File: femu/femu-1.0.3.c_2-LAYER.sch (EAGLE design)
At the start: 74 parts, among them IC1 ESP32-QFN_5X5

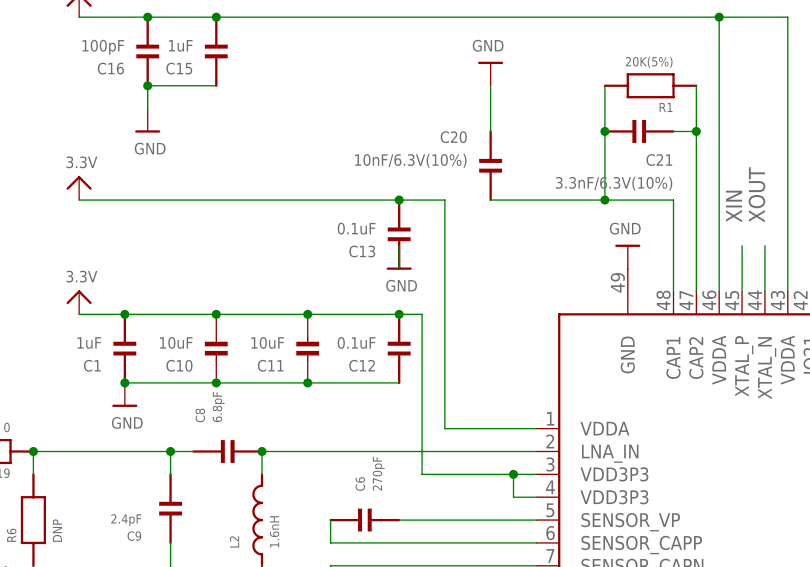
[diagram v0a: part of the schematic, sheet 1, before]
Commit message: Adding work on femu 1.0.2, and 1.0.3
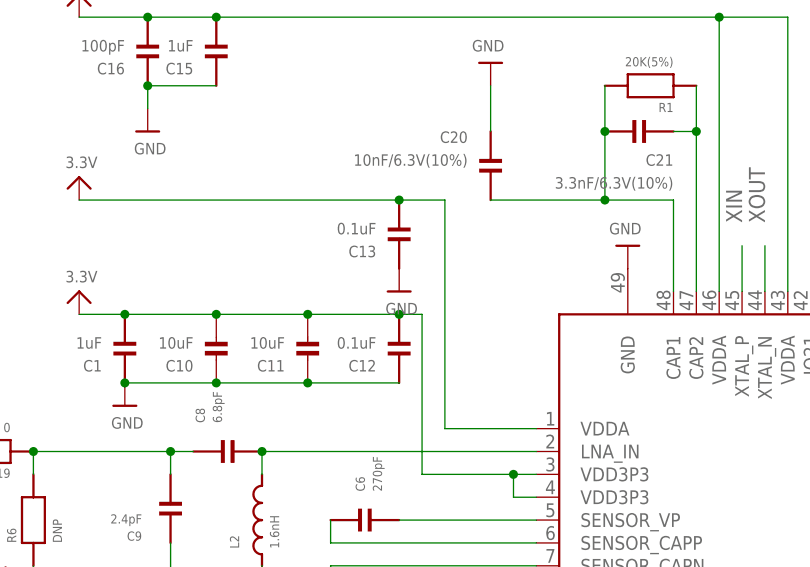
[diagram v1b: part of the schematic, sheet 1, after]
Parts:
- C13: MPN GRM022R60G104ME15L -> GRM033R61C104KE84D
- C23: MPN GRM035R60G475ME15D -> GRM035R60J475ME15D
- renumbered U$11 to IC2, U$57 to LDO2
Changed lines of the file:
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@@
 <part name="U$15" library="microbuilder" deviceset="GND" device=""/>
 <part name="C13" library="parts_0201" deviceset="CAPACITOR_0201" device="" value="0.1uF">
-<attribute name="MPN" value="GRM022R60G104ME15L"/>
+<attribute name="MPN" value="GRM033R61C104KE84D"/>
 </part>
 <part name="U$16" library="microbuilder" deviceset="GND" device=""/>
@@
 </part>
 <part name="C23" library="parts_0201" deviceset="CAPACITOR_0201" device="" value="4.7uF">
-<attribute name="MPN" value="GRM035R60G475ME15D"/>
+<attribute name="MPN" value="GRM035R60J475ME15D"/>
 </part>
 <part name="C24" library="parts_0201" deviceset="CAPACITOR_0201" device="" value="10nF">
@@
 <part name="U$17" library="microbuilder" deviceset="GND" device=""/>
 <part name="U$18" library="microbuilder" deviceset="3.3V" device=""/>
-<part name="U$11" library="ftdi_ft231x" deviceset="FT231XQ" device="">
+<part name="IC2" library="ftdi_ft231x" deviceset="FT231XQ" device="">
 <attribute name="MPN" value="FT231XQ"/>
 </part>
@@
 <attribute name="MPN" value="ERJ-1GN0R00C"/>
 </part>
-<part name="U$57" library="onsemi" deviceset="FAN25800AUC33X" device=""/>
+<part name="LDO2" library="onsemi" deviceset="FAN25800AUC33X" device=""/>
 <part name="R16" library="parts_0201" deviceset="RESISTOR_0201" device="" value="1K">
 <attribute name="MPN" value="RC0201FR-071KL"/>
@@
 <attribute name="MPN" x="99.06" y="154.94" size="1.778" layer="96" rot="R180" display="off"/>
 </instance>
-<instance part="U$16" gate="G$1" x="99.06" y="149.86" smashed="yes">
-<attribute name="VALUE" x="97.536" y="147.32" size="1.27" layer="96"/>
+<instance part="U$16" gate="G$1" x="99.06" y="147.32" smashed="yes">
+<attribute name="VALUE" x="97.536" y="144.78" size="1.27" layer="96"/>
 </instance>
 <instance part="C15" gate="G$1" x="78.74" y="175.26" smashed="yes" rot="R180">
@@
 <pinref part="C13" gate="G$1" pin="P$1"/>
 <pinref part="U$16" gate="G$1" pin="GND"/>
-<wire x1="99.06" y1="152.4" x2="99.06" y2="149.86" width="0.1524" layer="91"/>
 </segment>
 <segment>
@@
 <attribute name="MPN" x="193.04" y="137.16" size="1.778" layer="96" display="off"/>
 </instance>
-<instance part="U$57" gate="G$1" x="160.02" y="119.38" smashed="yes"/>
+<instance part="LDO2" gate="G$1" x="160.02" y="119.38" smashed="yes"/>
 <instance part="R16" gate="G$1" x="142.24" y="101.6" smashed="yes" rot="R90">
 <attribute name="NAME" x="140.335" y="101.6" size="1.016" layer="95" font="vector" rot="R90"/>
@@
 <pinref part="U$54" gate="G$1" pin="GND"/>
 <junction x="190.5" y="99.06"/>
-<pinref part="U$57" gate="G$1" pin="B2"/>
+<pinref part="LDO2" gate="G$1" pin="B2"/>
 <wire x1="175.26" y1="114.3" x2="175.26" y2="99.06" width="0.1524" layer="91"/>
 </segment>
@@
 <junction x="129.54" y="137.16"/>
 <pinref part="R16" gate="G$1" pin="1"/>
-<pinref part="U$57" gate="G$1" pin="A1"/>
+<pinref part="LDO2" gate="G$1" pin="A1"/>
 <wire x1="144.78" y1="137.16" x2="144.78" y2="124.46" width="0.1524" layer="91"/>
 </segment>
@@
 <pinref part="R13" gate="G$1" pin="1"/>
 <junction x="190.5" y="137.16"/>
-<pinref part="U$57" gate="G$1" pin="A2"/>
+<pinref part="LDO2" gate="G$1" pin="A2"/>
 <wire x1="175.26" y1="137.16" x2="175.26" y2="124.46" width="0.1524" layer="91"/>
 </segment>
@@
 <pinref part="R17" gate="G$1" pin="2"/>
 <wire x1="142.24" y1="109.22" x2="144.78" y2="109.22" width="0.1524" layer="91"/>
-<pinref part="U$57" gate="G$1" pin="B1"/>
+<pinref part="LDO2" gate="G$1" pin="B1"/>
 <wire x1="144.78" y1="109.22" x2="149.86" y2="109.22" width="0.1524" layer="91"/>
 <wire x1="144.78" y1="114.3" x2="144.78" y2="109.22" width="0.1524" layer="91"/>
@@
 <attribute name="VALUE" x="100.584" y="74.676" size="1.27" layer="96" rot="R90"/>
 </instance>
-<instance part="U$11" gate="G$1" x="142.24" y="142.24" smashed="yes">
+<instance part="IC2" gate="G$1" x="142.24" y="142.24" smashed="yes">
 <attribute name="MPN" x="142.24" y="142.24" size="1.778" layer="96" display="off"/>
 </instance>
@@
 </segment>
 <segment>
-<pinref part="U$11" gate="G$1" pin="USBDM"/>
+<pinref part="IC2" gate="G$1" pin="USBDM"/>
 <wire x1="119.38" y1="147.32" x2="111.76" y2="147.32" width="0.1524" layer="91"/>
 <label x="109.22" y="147.32" size="1.778" layer="95" rot="R180"/>
@@
 </segment>
 <segment>
-<pinref part="U$11" gate="G$1" pin="USBDP"/>
+<pinref part="IC2" gate="G$1" pin="USBDP"/>
 <wire x1="119.38" y1="144.78" x2="111.76" y2="144.78" width="0.1524" layer="91"/>
 <label x="109.22" y="144.78" size="1.778" layer="95" rot="R180"/>
@@
 </segment>
 <segment>
-<pinref part="U$11" gate="G$1" pin="GND@3"/>
+<pinref part="IC2" gate="G$1" pin="GND@3"/>
 <wire x1="139.7" y1="119.38" x2="139.7" y2="116.84" width="0.1524" layer="91"/>
 <wire x1="139.7" y1="116.84" x2="142.24" y2="116.84" width="0.1524" layer="91"/>
 <wire x1="142.24" y1="116.84" x2="142.24" y2="111.76" width="0.1524" layer="91"/>
-<pinref part="U$11" gate="G$1" pin="GND@21"/>
+<pinref part="IC2" gate="G$1" pin="GND@21"/>
 <wire x1="144.78" y1="119.38" x2="144.78" y2="116.84" width="0.1524" layer="91"/>
 <wire x1="144.78" y1="116.84" x2="142.24" y2="116.84" width="0.1524" layer="91"/>
 <junction x="142.24" y="116.84"/>
-<pinref part="U$11" gate="G$1" pin="GND@13"/>
+<pinref part="IC2" gate="G$1" pin="GND@13"/>
 <wire x1="142.24" y1="116.84" x2="142.24" y2="119.38" width="0.1524" layer="91"/>
 <pinref part="U$33" gate="G$1" pin="GND"/>
@@
 <net name="3.3V" class="0">
 <segment>
-<pinref part="U$11" gate="G$1" pin="3V3OUT"/>
+<pinref part="IC2" gate="G$1" pin="3V3OUT"/>
 <wire x1="119.38" y1="154.94" x2="116.84" y2="154.94" width="0.1524" layer="91"/>
-<pinref part="U$11" gate="G$1" pin="RESET#"/>
+<pinref part="IC2" gate="G$1" pin="RESET#"/>
 <wire x1="116.84" y1="154.94" x2="111.76" y2="154.94" width="0.1524" layer="91"/>
 <wire x1="119.38" y1="137.16" x2="116.84" y2="137.16" width="0.1524" layer="91"/>
 <wire x1="116.84" y1="137.16" x2="116.84" y2="154.94" width="0.1524" layer="91"/>
 <junction x="116.84" y="154.94"/>
-<pinref part="U$11" gate="G$1" pin="VCCIO"/>
+<pinref part="IC2" gate="G$1" pin="VCCIO"/>
 <wire x1="144.78" y1="165.1" x2="144.78" y2="177.8" width="0.1524" layer="91"/>
 <wire x1="144.78" y1="177.8" x2="116.84" y2="177.8" width="0.1524" layer="91"/>
@@
 <net name="EN/RTS" class="0">
 <segment>
-<pinref part="U$11" gate="G$1" pin="RTS"/>
+<pinref part="IC2" gate="G$1" pin="RTS"/>
 <wire x1="165.1" y1="152.4" x2="175.26" y2="152.4" width="0.1524" layer="91"/>
 <label x="177.8" y="152.4" size="1.778" layer="95"/>
@@
 <net name="BOOT/DTR" class="0">
 <segment>
-<pinref part="U$11" gate="G$1" pin="DTR"/>
+<pinref part="IC2" gate="G$1" pin="DTR"/>
 <wire x1="165.1" y1="147.32" x2="175.26" y2="147.32" width="0.1524" layer="91"/>
 <label x="177.8" y="147.32" size="1.778" layer="95"/>
@@
 <segment>
 <label x="177.8" y="157.48" size="1.778" layer="95"/>
-<pinref part="U$11" gate="G$1" pin="TXD"/>
+<pinref part="IC2" gate="G$1" pin="TXD"/>
 <wire x1="165.1" y1="157.48" x2="175.26" y2="157.48" width="0.1524" layer="91"/>
 </segment>
@@
 <wire x1="165.1" y1="154.94" x2="175.26" y2="154.94" width="0.1524" layer="91"/>
 <label x="177.8" y="154.94" size="1.778" layer="95"/>
-<pinref part="U$11" gate="G$1" pin="RXD"/>
+<pinref part="IC2" gate="G$1" pin="RXD"/>
 </segment>
 </net>
@@
 </segment>
 <segment>
-<pinref part="U$11" gate="G$1" pin="VCC"/>
+<pinref part="IC2" gate="G$1" pin="VCC"/>
 <pinref part="U$25" gate="G$1" pin="VIN"/>
 <wire x1="139.7" y1="165.1" x2="127" y2="165.1" width="0.1524" layer="91"/>
